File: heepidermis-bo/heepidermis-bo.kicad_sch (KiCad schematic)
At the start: 23 parts, among them J1 Conn_01x03, J10 Conn_Boaxial, J11 Conn_Boaxial, J12 Conn_01x03, J13 Conn_01x03, J14 Conn_01x03, J15 Conn_02x16_Odd_Even, J16 Conn_02x16_Odd_Even, J17 Conn_02x10_Odd_Even, J18 Conn_01x03, J19 Conn_01x03, J2 Conn_02x16_Odd_Even, J20 Conn_01x03, J21 Conn_01x03, J22 Conn_01x03, J3 Conn_02x16_Odd_Even, J4 Conn_02x16_Odd_Even, J5 Conn_01x03, J6 Conn_01x03, J7 Conn_01x03, J8 Conn_01x03, J9 Conn_Boaxial

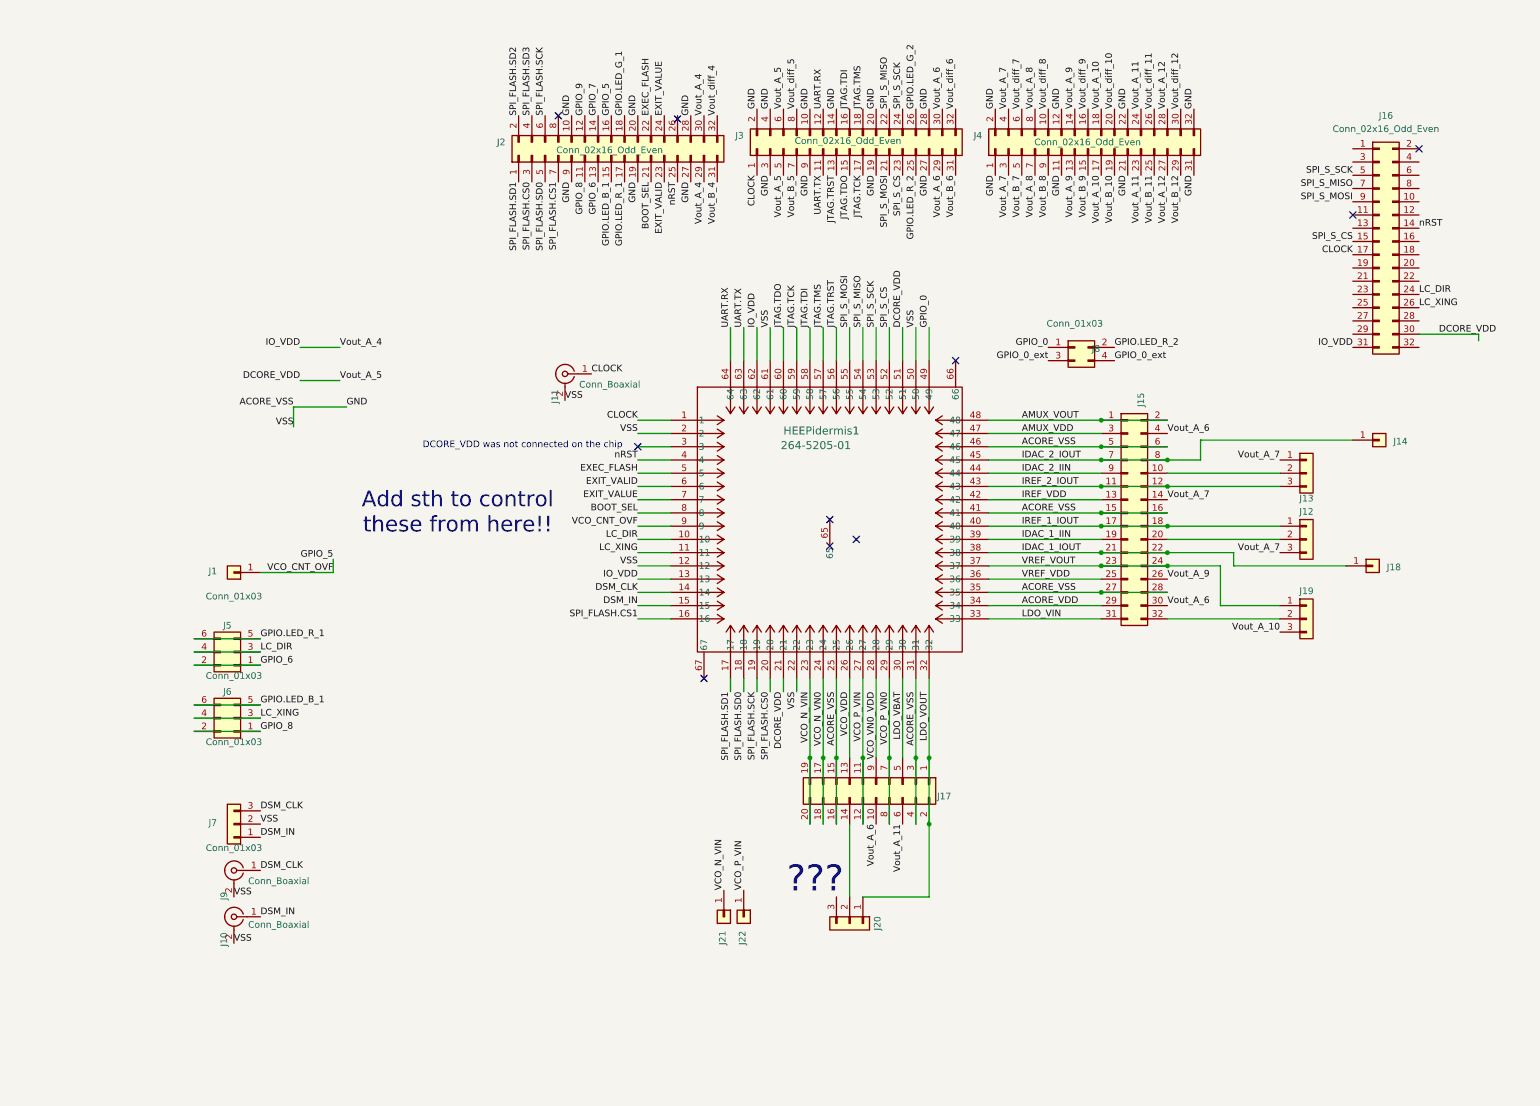
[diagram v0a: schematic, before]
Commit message: Finished adding the large connector. Missing gpios and qfn footprint
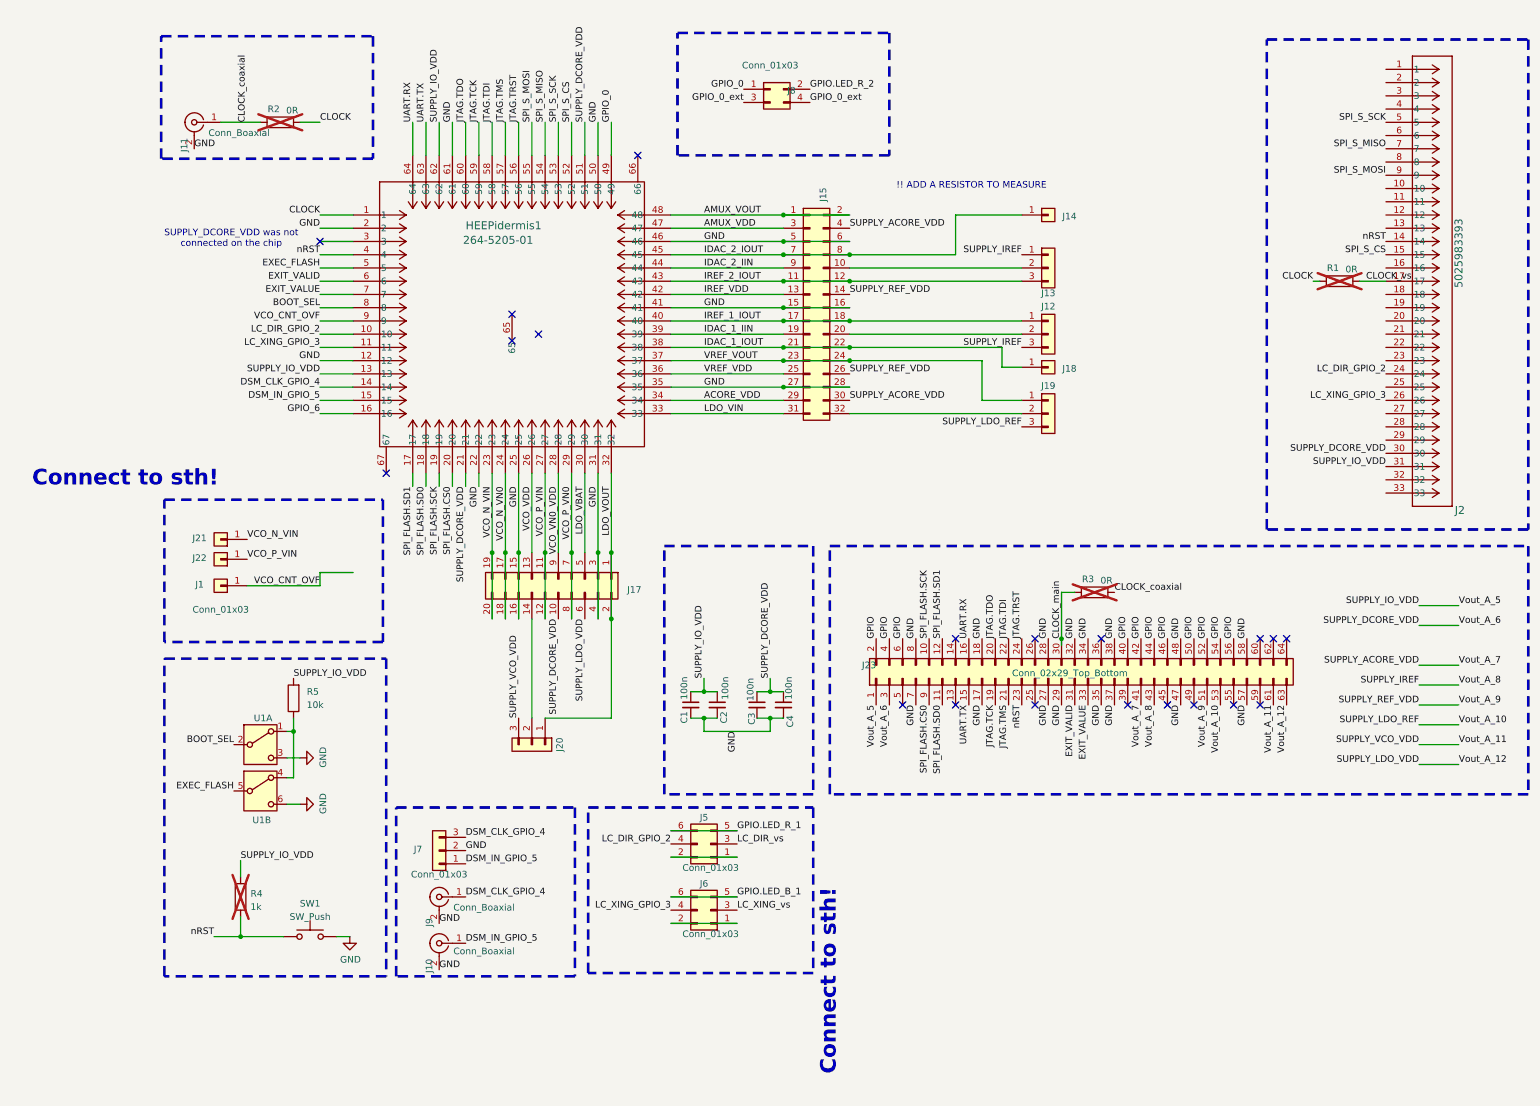
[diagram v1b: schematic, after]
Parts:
- removed J16, J2, J3, J4: Conn_02x16_Odd_Even, symbol Connector_Generic:Conn_02x16_Odd_Even
- added C1, C2, C3, C4: 100n, Capacitor_SMD:C_0603_1608Metric, symbol Device:C_Small
- added J2: 5025983393, heep_footprints:CONN_502598-3393_MOL, symbol 2025-09-27_11-33-13:5025983393
- added J23: Conn_02x29_Top_Bottom, Connector_PinHeader_2.54mm:PinHeader_2x32_P2.54mm_Vertical, symbol Connector_Generic:Conn_02x32_Odd_Even
- added R1, R2, R3: 0R, X-MODs_PcbLib:R0402, symbol Device:R
- added R4: 1k, Resistor_SMD:R_0603_1608Metric, symbol Device:R
- added R5: 10k, Resistor_SMD:R_0603_1608Metric, symbol Device:R
- added SW1: SW_Push, Button_Switch_SMD:SW_Push_1P1T_NO_CK_KMR2, symbol Switch:SW_Push
- added U1: ~, heep_footprints:SPDT-2pos-CAS-D20B1, symbol Switch:SW_DPDT_x2
- J15: footprint Connector_PinHeader_2.54mm:PinHeader_1x16_P2.54mm_Vertical -> Connector_PinHeader_2.54mm:PinHeader_02x16_P2.54mm_Vertical
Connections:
- net SPI_FLASH.CS1 is gone; now on net GPIO_6: HEEPidermis1.16
- net BOOT_SEL: now also U1.2 (B)
- net CLOCK: now also R1.1, R2.2; no longer J11.1 (In)
- net EXEC_FLASH: now also U1.5 (B)
- net EXIT_VALID: now also J23.31 (Pin_31)
- net EXIT_VALUE: now also J23.33 (Pin_33)
- net GPIO_6: no longer J5.1 (Pin_1), J5.2 (Pin_2)
- net JTAG.TCK: now also J23.19 (Pin_19)
- net JTAG.TDI: now also J23.22 (Pin_22)
- net JTAG.TDO: now also J23.20 (Pin_20)
- net JTAG.TMS: now also J23.21 (Pin_21)
- net JTAG.TRST: now also J23.24 (Pin_24)
- net SPI_FLASH.CS0: now also J23.9 (Pin_9)
- net SPI_FLASH.SCK: now also J23.10 (Pin_10)
- net SPI_FLASH.SD0: now also J23.11 (Pin_11)
- net SPI_FLASH.SD1: now also J23.12 (Pin_12)
- net SPI_S_CS: now also J2.15
- net SPI_S_MISO: now also J2.7
- net SPI_S_MOSI: now also J2.9
- net SPI_S_SCK: now also J2.5
- net UART.RX: now also J23.16 (Pin_16)
- net UART.TX: now also J23.15 (Pin_15)
- net nRST: now also J2.14, J23.23 (Pin_23), R4.1, SW1.1
- net SUPPLY_VCO_VDD: now reaches J20.3 (Pin_3)
- net SUPPLY_VCO_VDD: now also J23.61 (Pin_61)
- net ACORE_VSS renamed GND
- net GND: now also C1.2, C2.2, C3.2, C4.2, J23.17 (Pin_17), J23.18 (Pin_18), J23.27 (Pin_27), J23.28 (Pin_28), J23.29 (Pin_29), J23.32 (Pin_32), J23.34 (Pin_34), J23.35 (Pin_35), J23.37 (Pin_37), J23.38 (Pin_38), J23.47 (Pin_47), J23.48 (Pin_48), J23.57 (Pin_57), J23.58 (Pin_58), J23.7 (Pin_7), J23.8 (Pin_8), SW1.2, U1.3 (C), U1.6 (C)
- net DCORE_VDD renamed SUPPLY_DCORE_VDD
- net SUPPLY_DCORE_VDD: now also J17.10 (Pin_10), C3.1, C4.1, J2.30, J23.3 (Pin_3)
- net DSM_CLK renamed DSM_CLK_GPIO_4
- net DSM_IN renamed DSM_IN_GPIO_5
- net GPIO_5 renamed VCO_CNT_OVF
- net GPIO_8: no longer names the net of J6.1 (Pin_1), J6.2 (Pin_2)
- net IO_VDD renamed SUPPLY_IO_VDD
- net SUPPLY_IO_VDD: now also C1.1, C2.1, J2.31, J23.1 (Pin_1), R4.2, R5.2
- net LC_DIR renamed LC_DIR_GPIO_2
- net LC_DIR_GPIO_2: now also J2.24; no longer J5.3 (Pin_3)
- net LC_XING renamed LC_XING_GPIO_3
- net LC_XING_GPIO_3: now also J2.26; no longer J6.3 (Pin_3)
- net Vout_A_10 renamed SUPPLY_LDO_REF
- net SUPPLY_LDO_REF: now also J23.53 (Pin_53)
- net Vout_A_11 renamed SUPPLY_LDO_VDD
- net SUPPLY_LDO_VDD: now also J23.63 (Pin_63)
- net Vout_A_6 renamed SUPPLY_ACORE_VDD
- net SUPPLY_ACORE_VDD: now also J23.41 (Pin_41); no longer J17.10 (Pin_10)
- net Vout_A_7 renamed SUPPLY_IREF
- net SUPPLY_IREF: now also J23.43 (Pin_43); no longer J15.14 (Pin_14)
- net Vout_A_9 renamed SUPPLY_REF_VDD
- net SUPPLY_REF_VDD: now also J15.14 (Pin_14), J23.51 (Pin_51)
- new net: R5.1, U1.1 (A), U1.4 (A)
- new net: J5.1 (Pin_1), J5.2 (Pin_2)
- new net CLOCK_coaxial: J11.1 (In), R2.1, R3.2
- new net CLOCK_main: J23.30 (Pin_30), R3.1
- new net CLOCK_vs: J2.17, R1.2
- new net GPIO: J23.2 (Pin_2), J23.4 (Pin_4), J23.40 (Pin_40), J23.42 (Pin_42), J23.44 (Pin_44), J23.46 (Pin_46), J23.50 (Pin_50), J23.52 (Pin_52), J23.54 (Pin_54), J23.56 (Pin_56), J23.6 (Pin_6)
- new net LC_DIR_vs: J5.3 (Pin_3)
- new net LC_XING_vs: J6.3 (Pin_3)
- no-connect marks 10 -> 20
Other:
- note added: "!! ADD A RESISTOR TO MEASURE"
- note added: "Connect to sth!"
- note added: "SUPPLY_DCORE_VDD was not connected on the chip"
- note removed: "???"
- note removed: "Add sth to control these from here!!"
- note removed: "DCORE_VDD was not connected on the chip"
- moved on the sheet: HEEPidermis1, J1, J10, J11, J12, J13, J14, J15, J17, J18, J19, J20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

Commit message: Almost done adding footprint of qfn64
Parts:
- added HEEPidermis2: 264-5205-01, Package_DFN_QFN:QFN-64-1EP_9x9mm_P0.5mm_EP3.4x3.4mm, symbol QFN64-scoket:264-5205-01
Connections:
- net ACORE_VDD: now also HEEPidermis2.34
- net AMUX_VDD: now also HEEPidermis2.47
- net AMUX_VOUT: now also HEEPidermis2.48
- net BOOT_SEL: now also HEEPidermis2.8
- net CLOCK: now also HEEPidermis2.1
- net DSM_IN_GPIO_5: now also HEEPidermis2.15
- net EXEC_FLASH: now also HEEPidermis2.5
- net EXIT_VALID: now also HEEPidermis2.6
- net EXIT_VALUE: now also HEEPidermis2.7
- net GND: now also HEEPidermis2.12, HEEPidermis2.2, HEEPidermis2.22, HEEPidermis2.25, HEEPidermis2.31, HEEPidermis2.35, HEEPidermis2.41, HEEPidermis2.46, HEEPidermis2.50, HEEPidermis2.61
- net GPIO_0: now also HEEPidermis2.49
- net GPIO_6: now also HEEPidermis2.16
- net IDAC_1_IIN: now also HEEPidermis2.39
- net IDAC_1_IOUT: now also HEEPidermis2.38
- net IDAC_2_IIN: now also HEEPidermis2.44
- net IDAC_2_IOUT: now also HEEPidermis2.45
- net IREF_1_IOUT: now also HEEPidermis2.40
- net IREF_2_IOUT: now also HEEPidermis2.43
- net IREF_VDD: now also HEEPidermis2.42
- net JTAG.TCK: now also HEEPidermis2.59
- net JTAG.TDI: now also HEEPidermis2.58
- net JTAG.TDO: now also HEEPidermis2.60
- net JTAG.TMS: now also HEEPidermis2.57
- net JTAG.TRST: now also HEEPidermis2.56
- net LC_DIR_GPIO_2: now also HEEPidermis2.10
- net LC_XING_GPIO_3: now also HEEPidermis2.11
- net LDO_VBAT: now also HEEPidermis2.30
- net LDO_VIN: now also HEEPidermis2.33
- net LDO_VOUT: now also HEEPidermis2.32
- net SPI_FLASH.CS0: now also HEEPidermis2.20
- net SPI_FLASH.SCK: now also HEEPidermis2.19
- net SPI_FLASH.SD0: now also HEEPidermis2.18
- net SPI_FLASH.SD1: now also HEEPidermis2.17
- net SPI_S_CS: now also HEEPidermis2.52
- net SPI_S_MISO: now also HEEPidermis2.54
- net SPI_S_MOSI: now also HEEPidermis2.55
- net SPI_S_SCK: now also HEEPidermis2.53
- net SUPPLY_DCORE_VDD: now also HEEPidermis2.21, HEEPidermis2.51
- net SUPPLY_IO_VDD: now also HEEPidermis2.13, HEEPidermis2.62
- net UART.RX: now also HEEPidermis2.64
- net UART.TX: now also HEEPidermis2.63
- net VCO_CNT_OVF: now also HEEPidermis2.9
- net VCO_N_VIN: now also HEEPidermis2.23
- net VCO_N_VN0: now also HEEPidermis2.24
- net VCO_P_VIN: now also HEEPidermis2.27
- net VCO_P_VN0: now also HEEPidermis2.29
- net VCO_VDD: now also HEEPidermis2.26
- net VCO_VN0_VDD: now also HEEPidermis2.28
- net VREF_VDD: now also HEEPidermis2.36
- net VREF_VOUT: now also HEEPidermis2.37
- net nRST: now also HEEPidermis2.4
- no-connect marks 20 -> 21

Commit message: DRC clean
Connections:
- net DSM_IN_GPIO_5: no longer HEEPidermis2.15
- net EXIT_VALID: no longer HEEPidermis2.6
- net EXIT_VALUE: no longer HEEPidermis2.7
- net GPIO.LED_B_1: now also J23.6 (Pin_6)
- net GPIO.LED_R_1: now also J23.4 (Pin_4)
- net GPIO.LED_R_2: now also J23.40 (Pin_40)
- net GPIO_0: no longer HEEPidermis2.49
- net GPIO_6: now also J23.2 (Pin_2)
- net LC_DIR_GPIO_2: no longer J2.24
- net LC_DIR_vs: now also J2.24
- net LC_XING_GPIO_3: no longer J2.26
- net LC_XING_vs: now also J2.26
- net VCO_CNT_OVF: no longer HEEPidermis2.9
- net VCO_N_VN0: no longer HEEPidermis2.24
- net VCO_P_VN0: no longer HEEPidermis2.29
- net VCO_VN0_VDD: no longer HEEPidermis2.28
- removed net GPIO: J23.2 (Pin_2), J23.4 (Pin_4), J23.40 (Pin_40), J23.42 (Pin_42), J23.44 (Pin_44), J23.46 (Pin_46), J23.50 (Pin_50), J23.52 (Pin_52), J23.54 (Pin_54), J23.56 (Pin_56), J23.6 (Pin_6)
- no-connect marks 21 -> 63
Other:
- note added: "ADD GND TEST POINTS"
- note added: "ADD SPI S TEST POINTS"
- note added: "ADD versasens TEST POINTS"
- moved on the sheet: R3

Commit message: Uploaded gerbers
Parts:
- added J16, J24, J25, J26, J27, J28, J29, J3, J30, J31, J32, J33, J34, J35, J36, J4: Conn_01x03, TestPoint_THTPad_1.0x1.0mm_Drill0.5mm, symbol Connector_Generic:Conn_01x01
- added R6, R7: 0R, Resistor_SMD:R_0402_1005Metric, symbol Device:R
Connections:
- net CLOCK_vs: now also J36.1 (Pin_1)
- net GND: now also J29.1 (Pin_1), J30.1 (Pin_1)
- net IDAC_1_IOUT: now also R7.1; no longer J18.1 (Pin_1)
- net IDAC_2_IOUT: now also R6.1; no longer J14.1 (Pin_1)
- net LC_DIR_vs: now also J34.1 (Pin_1)
- net LC_XING_vs: now also J35.1 (Pin_1)
- net SPI_FLASH.CS0: now also J24.1 (Pin_1)
- net SPI_FLASH.SCK: now also J16.1 (Pin_1)
- net SPI_FLASH.SD0: now also J4.1 (Pin_1)
- net SPI_FLASH.SD1: now also J3.1 (Pin_1)
- net SPI_S_CS: now also J25.1 (Pin_1)
- net SPI_S_MISO: now also J27.1 (Pin_1)
- net SPI_S_MOSI: now also J28.1 (Pin_1)
- net SPI_S_SCK: now also J26.1 (Pin_1)
- net SUPPLY_DCORE_VDD: now also J32.1 (Pin_1)
- net SUPPLY_IO_VDD: now also J31.1 (Pin_1)
- net nRST: now also J33.1 (Pin_1)
- new net: J14.1 (Pin_1), R6.2
- new net: J18.1 (Pin_1), R7.2
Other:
- note added: "!! ADD A RESISTOR TO MEASURE current from iOUT"
- note removed: "!! ADD A RESISTOR TO MEASURE"
- note removed: "ADD GND TEST POINTS"
- note removed: "ADD SPI S TEST POINTS"
- note removed: "ADD versasens TEST POINTS"
- note removed: "Connect to sth!"

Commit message: Added zskin
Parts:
- added C10, C5, C6, C7, C8, C9: 100n, Capacitor_SMD:C_0603_1608Metric, symbol Device:C_Small
- added C11: Cp_skin, Capacitor_SMD:C_0603_1608Metric, symbol Device:C_Small
- added J37: Conn_01x02, Connector_PinHeader_1.27mm:PinHeader_1x04_P1.27mm_Vertical, symbol Connector_Generic:Conn_01x04
- added R8: Rs_skin, Resistor_SMD:R_0603_1608Metric, symbol Device:R
- added R9: Rp_skin, Resistor_SMD:R_0603_1608Metric, symbol Device:R
- renumbered C3 to C2, C2 to C3
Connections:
- net GND: now also C10.2, C5.2, C6.2, C7.2, C8.2, C9.2
- net SUPPLY_ACORE_VDD: now also C10.1
- net SUPPLY_IREF: now also C9.1
- net SUPPLY_LDO_REF: now also C7.1
- net SUPPLY_LDO_VDD: now also C5.1
- net SUPPLY_REF_VDD: now also C8.1
- net SUPPLY_VCO_VDD: now also C6.1
- net VCO_P_VIN: now also J37.2 (Pin_2), J37.3 (Pin_3)
- net VCO_VDD_SEL: now reaches J17.14 (Pin_14), J20.2 (Pin_2)
- net VCO_VDD_SEL: now also R8.2
- net iDAC1_inj: now reaches J18.1 (Pin_1), R7.2
- net iDAC1_inj: now also J37.4 (Pin_4)
- new net: C11.2, J37.1 (Pin_1), R9.1
- new net: C11.1, R8.1, R9.2
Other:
- moved on the sheet: J20
